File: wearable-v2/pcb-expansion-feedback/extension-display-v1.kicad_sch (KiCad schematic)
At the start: 30 parts, among them J16 EA_WF030-39S, J17 JST_AUDIO_OUT, J18 DEBUG_HERALD, J19 FTDI_HERALD, J9 HERALD_V2_CONN_PLUG, U10 ATmega328PB-M, U13 TPA6139A2RGTR, U16 DRV2605LDGSR, U17 VG0832013D, U7 MX25R6435FZNIL0, Y2 8Mhz

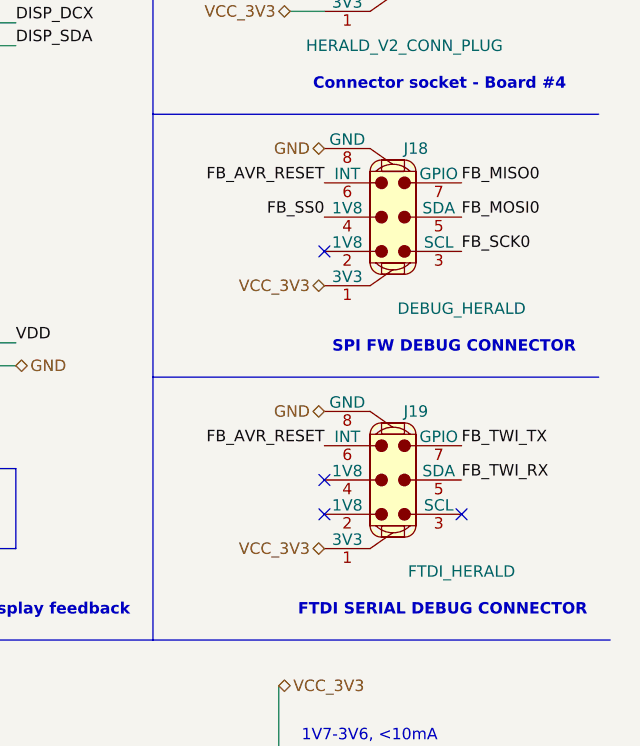
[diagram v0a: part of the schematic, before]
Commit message: Refactoring PCB files
Moved major boards into their own files.
Corrected design elements for PCBWay manufacture.
Signed-off-by: Adam Fowler <adam@adamfowler.org>
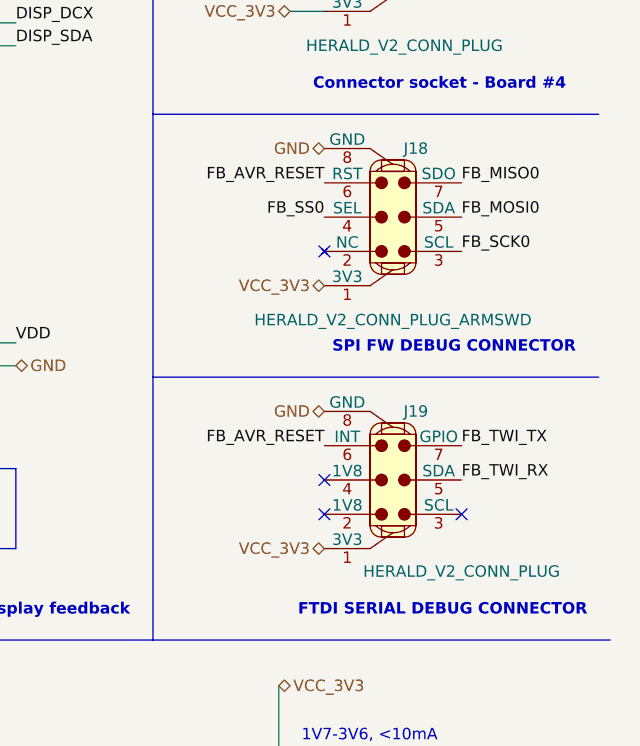
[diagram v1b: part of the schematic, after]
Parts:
- J18: value DEBUG_HERALD -> HERALD_V2_CONN_PLUG_ARMSWD; footprint Herald:HERALD_V2_CONN_PORT -> (none); symbol Herald_Extras:HERALD_V2_CONN_PLUG -> Herald_Extras:HERALD_V2_CONN_PLUG_ARMSWD; MPN (none) -> 145861006024829+
- J19: value FTDI_HERALD -> HERALD_V2_CONN_PLUG; MPN (none) -> 145861006024829+
- J9: MPN (none) -> 145861006024829+
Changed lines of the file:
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@@
     )
   )
-  (symbol (lib_id "Herald_Extras:HERALD_V2_CONN_PLUG") (at 260.35 34.29 0) (unit 1)
+  (symbol (lib_name "HERALD_V2_CONN_PLUG_1") (lib_id "Herald_Extras:HERALD_V2_CONN_PLUG") (at 260.35 34.29 0) (unit 1)
     (in_bom yes) (on_board yes) (dnp no)
     (property "Reference" "J9" (at 260.35 22.86 0)
@@
     )
     (property "Datasheet" "https://ele.kyocera.com/assets/products/connector/specification/201035861003.pdf" (at 261.62 49.53 0)
+      (effects (font (size 1.27 1.27)) hide)
+    )
+    (property "MPN" "145861006024829+" (at 260.35 60.96 0)
       (effects (font (size 1.27 1.27)) hide)
     )
@@
       (effects (font (size 1.27 1.27)))
     )
-    (property "Value" "FTDI_HERALD" (at 267.97 104.14 0)
+    (property "Value" "HERALD_V2_CONN_PLUG" (at 267.97 104.14 0)
       (effects (font (size 1.27 1.27)))
     )
@@
     )
     (property "Datasheet" "https://ele.kyocera.com/assets/products/connector/specification/201035861003.pdf" (at 261.62 109.22 0)
+      (effects (font (size 1.27 1.27)) hide)
+    )
+    (property "MPN" "145861006024829+" (at 260.35 120.65 0)
       (effects (font (size 1.27 1.27)) hide)
     )
@@
     )
   )
-  (symbol (lib_id "Herald_Extras:HERALD_V2_CONN_PLUG") (at 260.35 64.77 0) (unit 1)
+  (symbol (lib_id "Herald_Extras:HERALD_V2_CONN_PLUG_ARMSWD") (at 260.35 64.77 0) (unit 1)
     (in_bom yes) (on_board yes) (dnp no)
     (property "Reference" "J18" (at 262.89 57.15 0)
       (effects (font (size 1.27 1.27)))
     )
-    (property "Value" "DEBUG_HERALD" (at 267.97 74.93 0)
-      (effects (font (size 1.27 1.27)))
-    )
-    (property "Footprint" "Herald:HERALD_V2_CONN_PORT" (at 260.35 60.96 0)
+    (property "Value" "HERALD_V2_CONN_PLUG_ARMSWD" (at 260.35 76.2 0)
+      (effects (font (size 1.27 1.27)))
+    )
+    (property "Footprint" "" (at 260.35 60.96 0)
       (effects (font (size 1.27 1.27)) hide)
     )
@@
       (effects (font (size 1.27 1.27)) hide)
     )
+    (property "MPN" "145861006024829+" (at 260.35 83.82 0)
+      (effects (font (size 1.27 1.27)) hide)
+    )

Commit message: Reworked boards for JLCPCB manufacture
Slightly larger Vias.
Added debug pin holes for Beta testing.
Signed-off-by: Adam Fowler <adam@adamfowler.org>
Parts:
- U17: footprint (none) -> Connector_PinHeader_1.00mm:PinHeader_1x02_P1.00mm_Vertical
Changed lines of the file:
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@@
       (effects (font (size 1.27 1.27)) (justify left))
     )
-    (property "Footprint" "" (at 119.38 133.35 0)
+    (property "Footprint" "Connector_PinHeader_1.00mm:PinHeader_1x02_P1.00mm_Vertical" (at 119.38 133.35 0)
       (effects (font (size 1.27 1.27)) hide)
     )
